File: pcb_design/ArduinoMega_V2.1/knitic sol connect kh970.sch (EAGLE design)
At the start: 18 parts

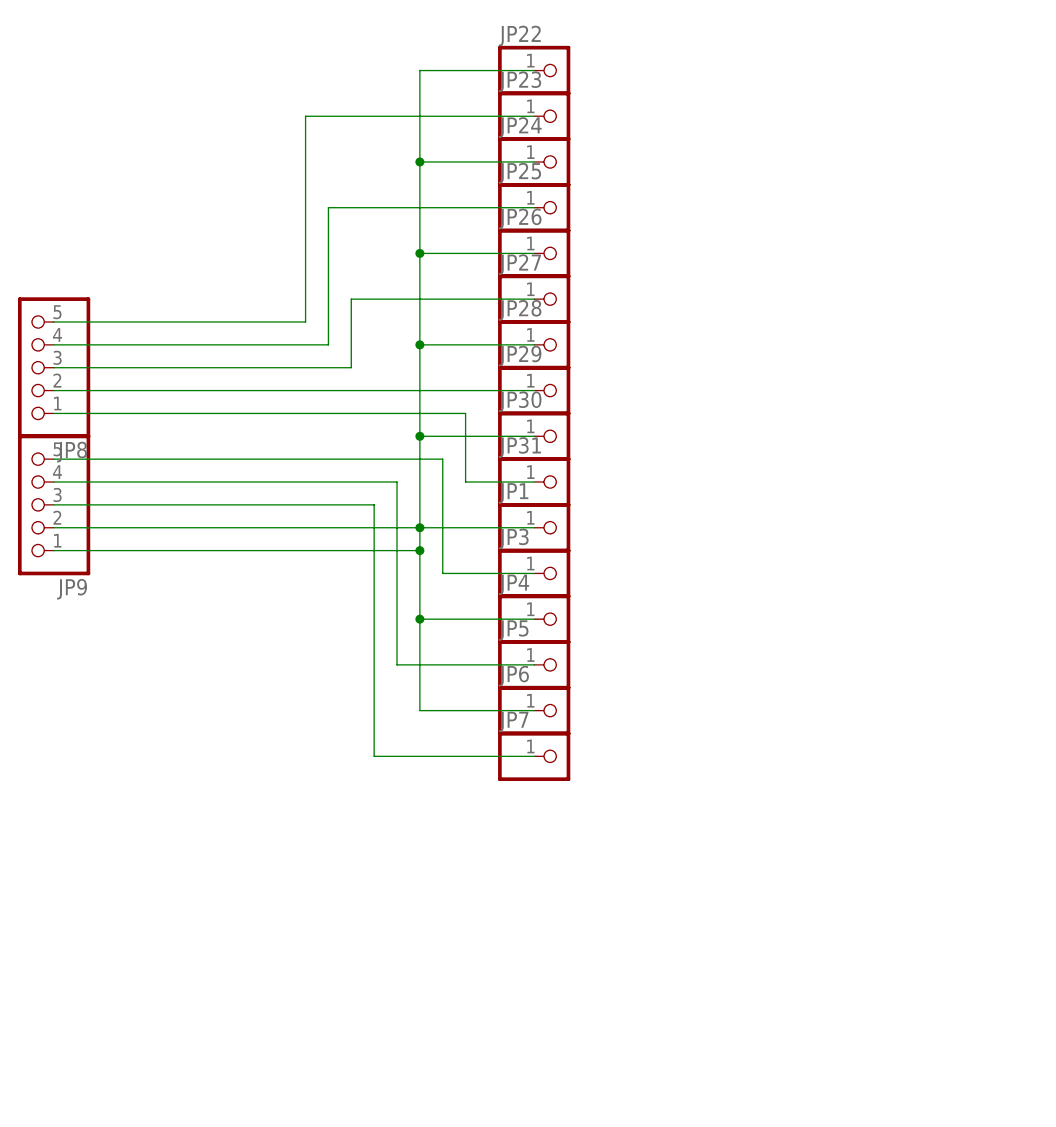
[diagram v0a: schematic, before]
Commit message: Add info and reset/led on pcb design
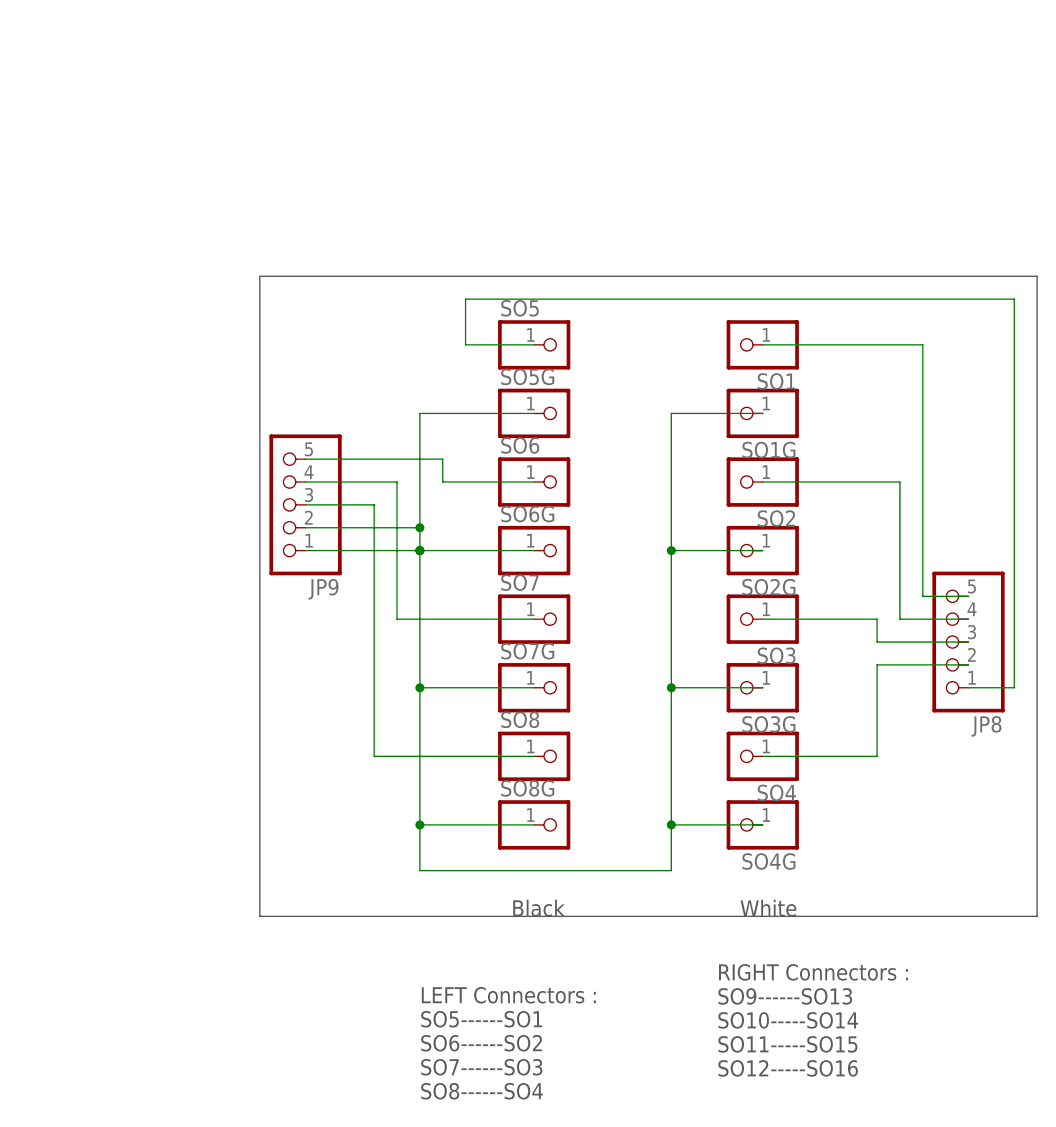
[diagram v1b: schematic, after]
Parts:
- removed JP1, JP22, JP23, JP24, JP25, JP26, JP27, JP29, JP3, JP30, JP5, JP6: (no value), pinhead:PINHD-1X1
- added SO1, SO1G, SO2, SO2G, SO3, SO3G, SO4, SO4G, SO5G, SO6G, SO7G, SO8G: (no value), pinhead:PINHD-1X1
- renumbered JP28 to SO5, JP31 to SO6, JP4 to SO7, JP7 to SO8
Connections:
- removed net N$1: JP1.1, JP22.1, JP24.1, JP26.1, JP30.1, JP6.1, JP9.1, JP9.2, SO5.1, SO7.1
- removed net N$4: JP3.1, JP9.5
- new net N$10: JP9.1, JP9.2, SO1G.1, SO2G.1, SO3G.1, SO4G.1, SO5G.1, SO6G.1, SO7G.1, SO8G.1
- new net SO6G: JP9.5, SO6.1
- net N$3: now also SO7.1; no longer JP5.1
- net N$5: now also SO5.1; no longer SO6.1
- net N$6: now also JP8.5, SO1.1; no longer JP29.1, JP8.2
- net N$7: now also JP8.4, SO2.1; no longer JP27.1, JP8.3
- net N$8: now also JP8.3, SO3.1; no longer JP25.1, JP8.4
- net N$9: now also JP8.2, SO4.1; no longer JP23.1, JP8.5
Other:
- note added: "Black"
- note added: "LEFT Connectors : SO5------SO1 SO6------SO2 SO7------SO3 SO8------SO4"
- note added: "RIGHT Connectors : SO9------SO13 SO10-----SO14 SO11-----SO15 SO12-----SO16"
- note added: "White"
- moved on the sheet: JP8, JP9
